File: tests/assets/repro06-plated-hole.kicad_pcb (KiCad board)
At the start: 2 copper layers, 50 x 50 mm, 2 parts

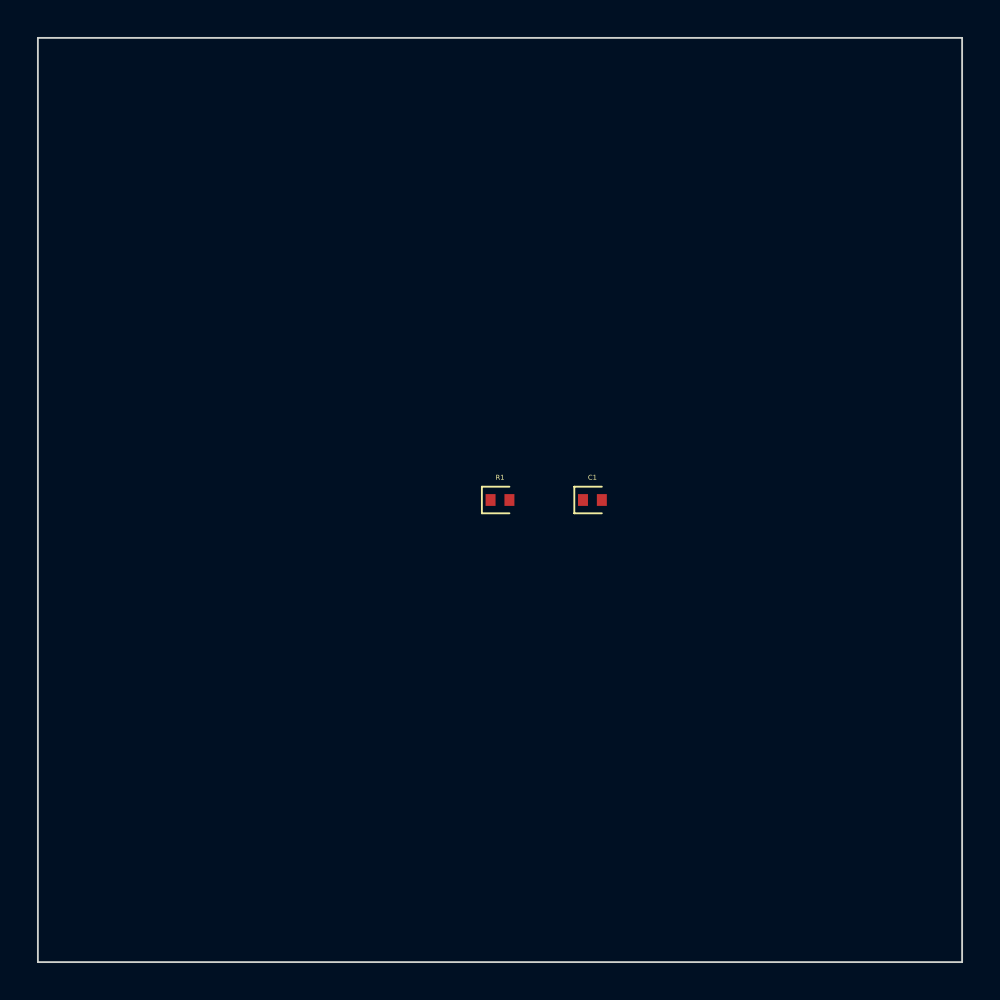
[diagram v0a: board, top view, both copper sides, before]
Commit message: fix: add support for standalone plated holes in KiCad PCB converter
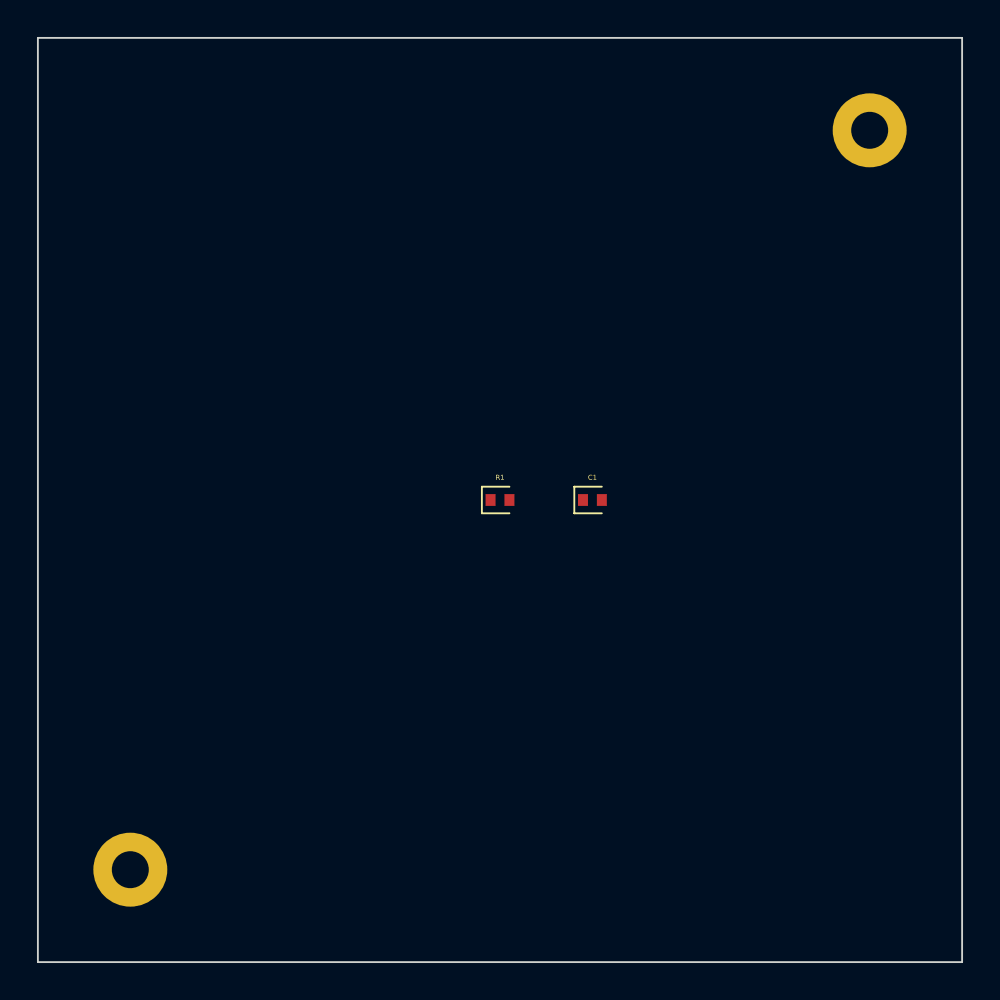
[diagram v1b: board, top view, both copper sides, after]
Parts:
- added ? (x2): , tscircuit:MountingHole_Pad, F.Cu at (100.0, 100.0)
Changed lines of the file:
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@@
+    )
+  )
+  (footprint
+    "tscircuit:MountingHole_Pad"
+    (layer F.Cu)
+    (at 100 100 0)
+    (pad "1" thru_hole circle
+      (at -20 20 0)
+      (size 4 4)
+      (drill 2)
+      (layers *.Cu *.Mask)
+    )
+  )
+  (footprint
+    "tscircuit:MountingHole_Pad"
+    (layer F.Cu)
+    (at 100 100 0)
+    (pad "1" thru_hole circle
+      (at 20 -20 0)
+      (size 4 4)
+      (drill 2)
+      (layers *.Cu *.Mask)
     )
   )

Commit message: up
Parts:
- ? (x2): footprint tscircuit:MountingHole_Pad -> tscircuit:platedhole_circle_holeDiameter2mm_outerDiameter4mm
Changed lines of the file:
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@@
   )
   (footprint
-    "tscircuit:MountingHole_Pad"
+    "tscircuit:platedhole_circle_holeDiameter2mm_outerDiameter4mm"
     (layer F.Cu)
     (at 100 100 0)
@@
   )
   (footprint
-    "tscircuit:MountingHole_Pad"
+    "tscircuit:platedhole_circle_holeDiameter2mm_outerDiameter4mm"
     (layer F.Cu)
     (at 100 100 0)
